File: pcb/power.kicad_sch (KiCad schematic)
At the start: 39 parts, among them J2 USB_C_Top, J3 USB_C_Bottom, Q2 AO3401A, Q3 AO3400A, Q4 AO3400A, U2 TPS63000, U3 TPS63000, U4 TP4056, U5 DW01A

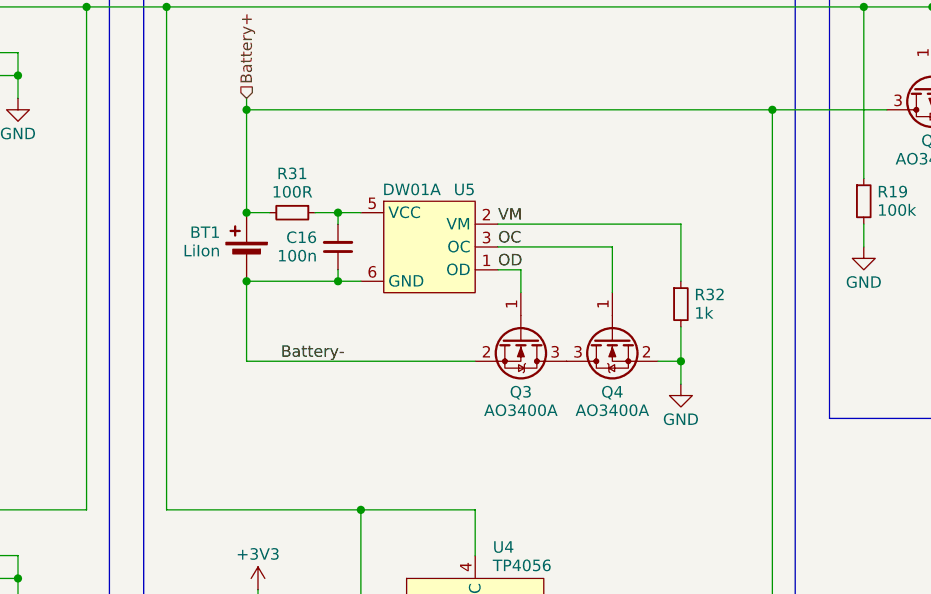
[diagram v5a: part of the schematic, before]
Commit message: fix: add missing JLC part numbers
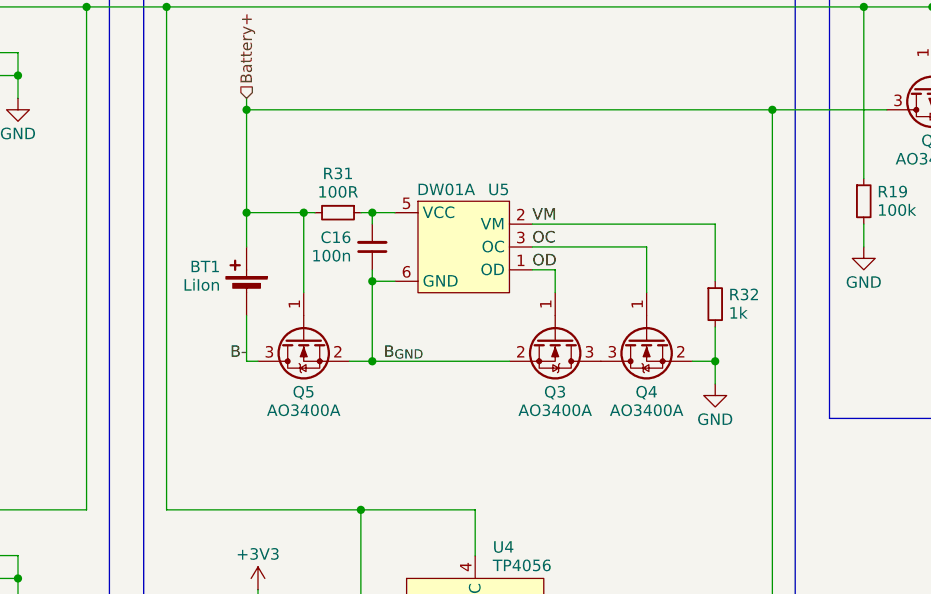
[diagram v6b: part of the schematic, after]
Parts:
- added Q5: AO3400A, Package_TO_SOT_SMD:SOT-23, symbol Transistor_FET:AO3400A
- C14, C15, C16: LCSC (none) -> C1525
- Q3, Q4: LCSC (none) -> C20917
- R18: LCSC C25744 -> C4109
- R29, R30, R31: LCSC (none) -> C25076
- R32: LCSC (none) -> C11702
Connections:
- net Battery+: now also Q5.1 (G)
- net Battery- renamed B_{GND}
- net B_{GND}: now also Q5.2 (S); no longer BT1.2 (-)
- new net B-: BT1.2 (-), Q5.3 (D)
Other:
- moved on the sheet: BT1, C16, Q3, Q4, R31, R32, U5

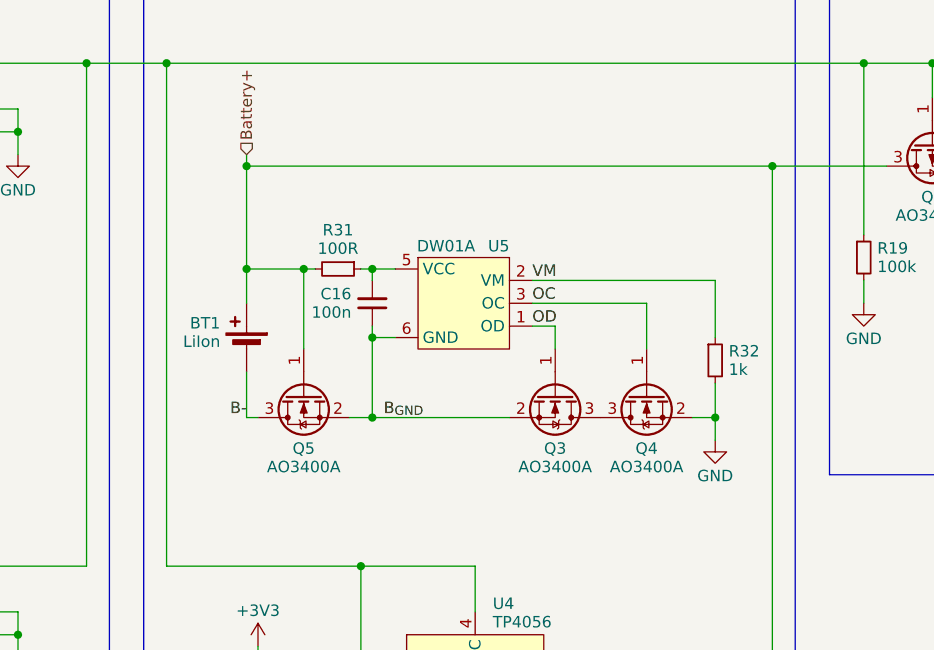
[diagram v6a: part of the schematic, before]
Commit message: feat: remove battery protection IC
Since I only use protected battery packs (which is highly recommended) the additional protection IC on the PCB was obsolete and only raised production cost.
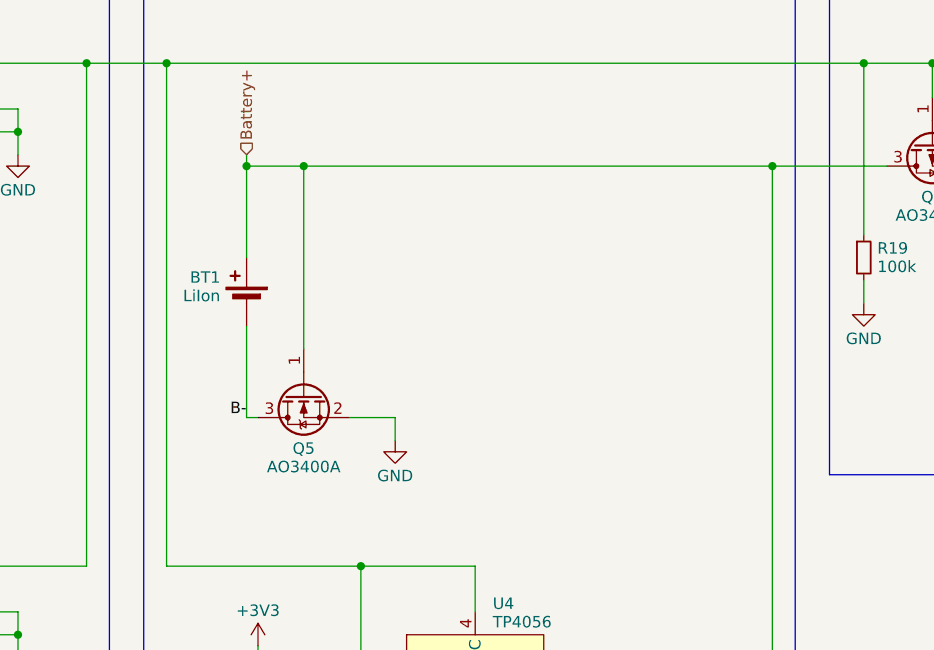
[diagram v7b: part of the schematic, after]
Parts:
- removed C16: 100n, Capacitor_SMD:C_0402_1005Metric, symbol Device:C_Small
- removed Q3, Q4: AO3400A, Package_TO_SOT_SMD:SOT-23, symbol Transistor_FET:AO3400A
- removed R31: 100R, Resistor_SMD:R_0402_1005Metric, symbol Device:R_Small
- removed R32: 1k, Resistor_SMD:R_0402_1005Metric, symbol Device:R_Small
- removed U5: DW01A, Package_TO_SOT_SMD:SOT-23-6, symbol My_Symbols:DW01A
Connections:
- net B_{GND} is gone; now on net GND: Q5.2 (S)
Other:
- moved on the sheet: BT1

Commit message: feat: replace TP4056 Prog Resistor footprint with 0603
Replace the footprint for the programming resistor to 0603 to make replacing it easier. Also changing the default value to 4.7k for slower charge and less heat production
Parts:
- R18: value 2k -> 4k7; footprint Resistor_SMD:R_0402_1005Metric -> Resistor_SMD:R_0603_1608Metric_Pad0.98x0.95mm_HandSolder; LCSC C4109 -> C23162
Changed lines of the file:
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@@
       (effects (font (size 1.27 1.27)) (justify left))
     )
-    (property "Value" "2k" (at 133.5786 124.214 0)
+    (property "Value" "4k7" (at 133.5786 124.214 0)
       (effects (font (size 1.27 1.27)) (justify left))
     )
-    (property "Footprint" "Resistor_SMD:R_0402_1005Metric" (at 132.08 123.19 0)
+    (property "Footprint" "Resistor_SMD:R_0603_1608Metric_Pad0.98x0.95mm_HandSolder" (at 132.08 123.19 0)
       (effects (font (size 1.27 1.27)) hide)
     )
@@
       (effects (font (size 1.27 1.27)) hide)
     )
-    (property "LCSC" "C4109" (at 132.08 123.19 0)
+    (property "LCSC" "C23162" (at 132.08 123.19 0)
       (effects (font (size 1.27 1.27)) hide)
     )
